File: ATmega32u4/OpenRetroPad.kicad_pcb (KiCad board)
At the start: 4 copper layers, 46 x 74 mm, 48 parts, among them J1 USB_B_Micro, J2 NRF24, J3 DB25_Female_MountingHoles, SW1 SW_Push, SW2 SW_Push, U1 AMS1117-3.3, U2 ATmega32U4, Y1 16MHz

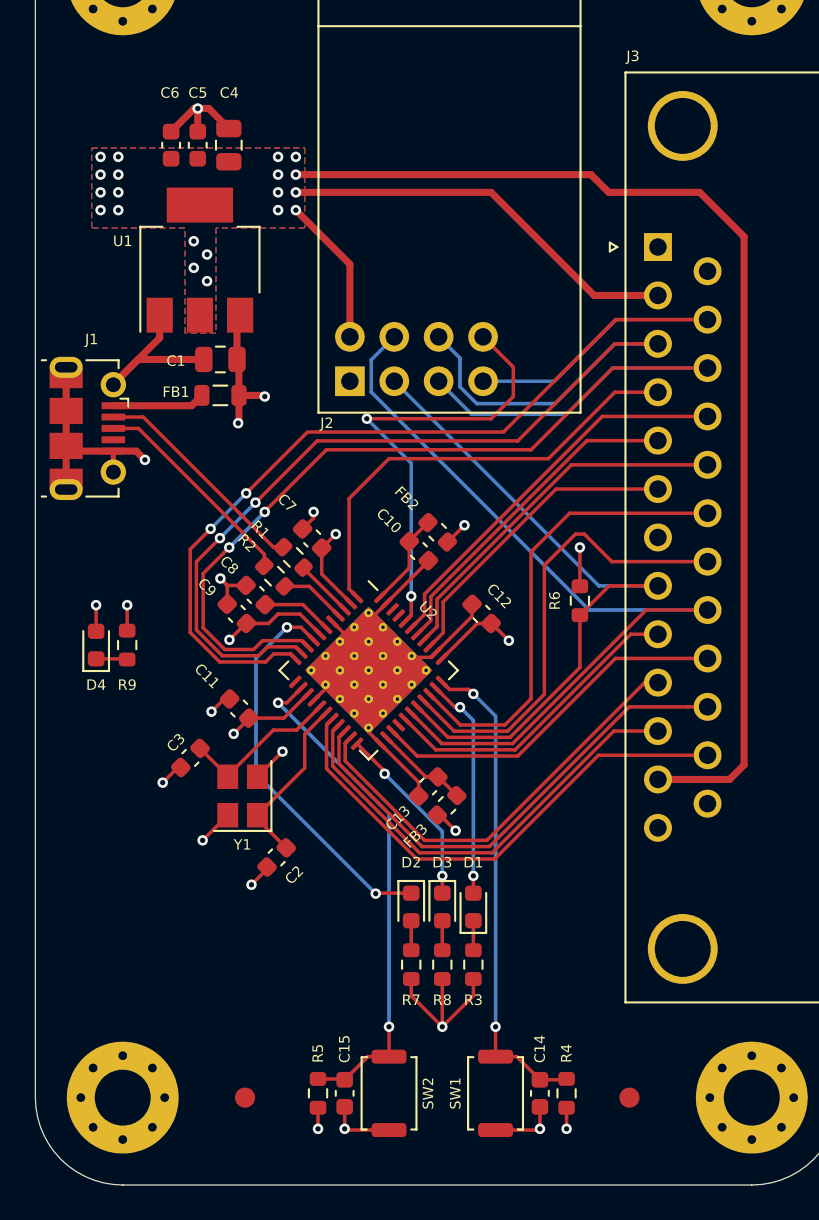
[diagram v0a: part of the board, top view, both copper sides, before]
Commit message: Update layout around MicroUSB connector, add teardrops
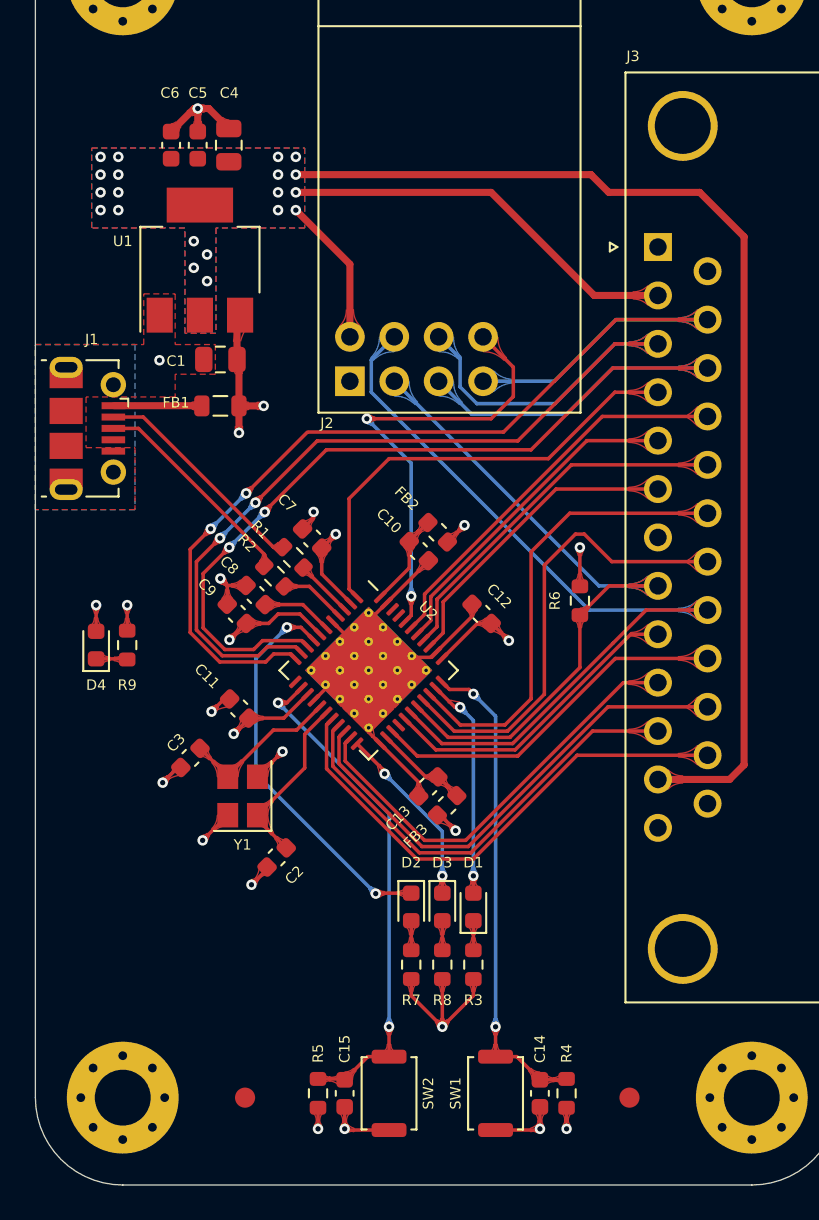
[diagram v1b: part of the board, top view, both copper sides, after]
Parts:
- moved FB1 0.60 mm to (117.3, 86.6)
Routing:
- net GND: track 91.2 -> 68.6 mm
- added copper zone on B.Cu, net GND
- added copper zone on F.Cu, net GND

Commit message: Update text on back to include domain name instead of github link
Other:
- board text added: "OpenRetroPad ATmega32u4 v1 JAN-21 OpenRetroPad.com"
- board text removed: "OpenRetroPad ATmega32u4 v1 JAN-21 github.com/OpenRetroPad"

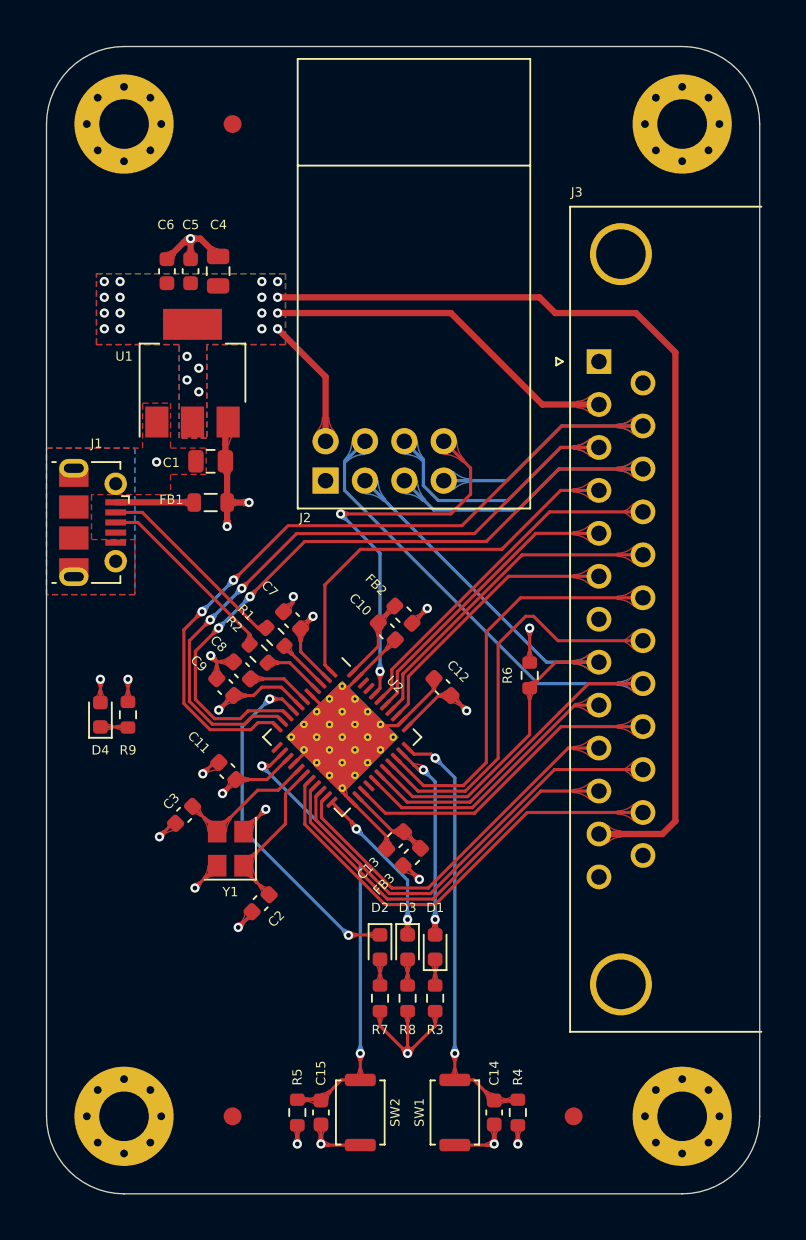
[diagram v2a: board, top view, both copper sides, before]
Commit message: Convert from 4 layer to 2 layer board
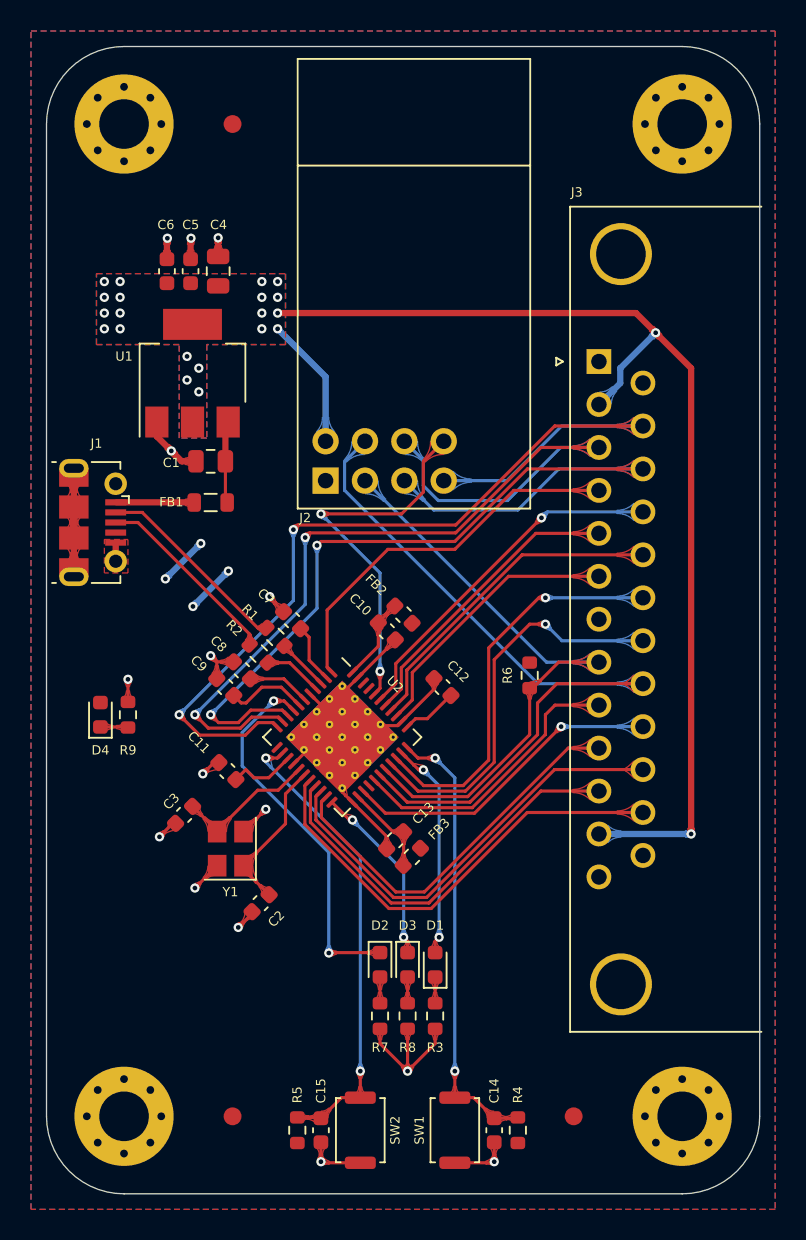
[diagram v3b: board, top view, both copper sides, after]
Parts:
- moved C14 1.14 mm to (135.6, 127.1)
- moved C15 1.14 mm to (124.5, 127.1)
- moved D1 1.14 mm to (131.8, 116.5)
- moved D2 1.14 mm to (128.3, 116.5)
- moved D3 1.14 mm to (130.0, 116.5)
- moved R3 1.14 mm to (131.8, 119.8)
- moved R4 1.14 mm to (137.2, 127.1)
- moved R5 1.14 mm to (122.9, 127.1)
- moved R7 1.14 mm to (128.3, 119.8)
- moved R8 1.14 mm to (130.0, 119.8)
- moved SW1 1.14 mm to (133.1, 127.1)
- moved SW2 1.14 mm to (127.0, 127.1)
- turned FB3 to 225 degrees
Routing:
- net +3V3: track 94.3 -> 78.8 mm, vias 20 -> 22
- net +5V: track 38.7 -> 28.9 mm, vias 12 -> 4
- net GND: track 68.6 -> 78.1 mm, vias 13 -> 15
- net PB0: track 22.7 -> 24.3 mm
- net PF1: track 25.9 -> 24.4 mm
- net PC7: track 12.8 -> 14.2 mm
- net PD5: track 10.6 -> 11.8 mm
- net PB4: track 49.0 -> 50.2 mm
- net PB1: track 61.0 -> 59.8 mm
- net PE6: track 26.0 -> 24.9 mm
- net PE2: track 28.0 -> 29.1 mm
- net RESET: track 29.2 -> 30.3 mm
- net PB3: track 61.0 -> 61.9 mm
- net PB6: track 26.6 -> 25.8 mm, vias 0 -> 1
- net PD7: track 18.0 -> 18.7 mm
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- added copper zone on F.Cu, net +5V
- removed copper zone on In2.Cu, net +5V
- removed copper zone on In1.Cu, net GND
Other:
- copper layers 4 -> 2

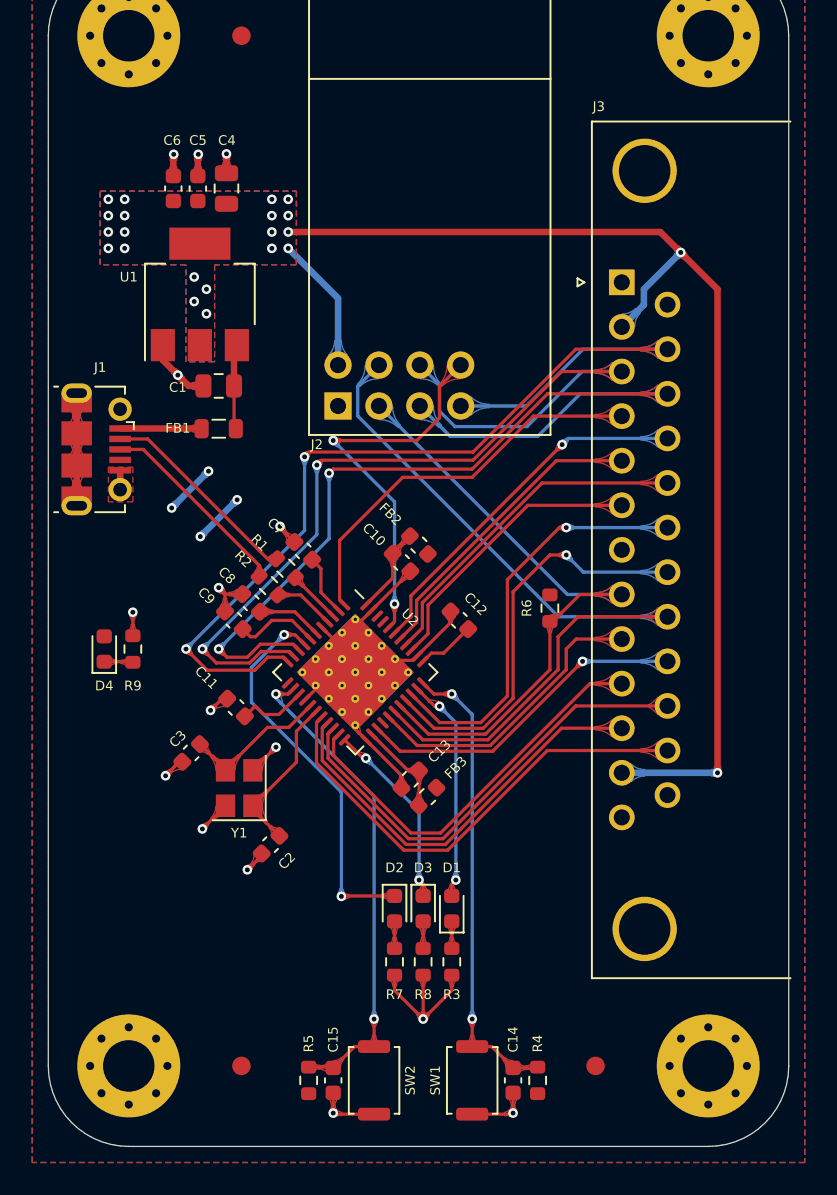
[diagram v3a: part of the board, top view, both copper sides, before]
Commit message: Update 2 layer board and use 0805 components, include outputs
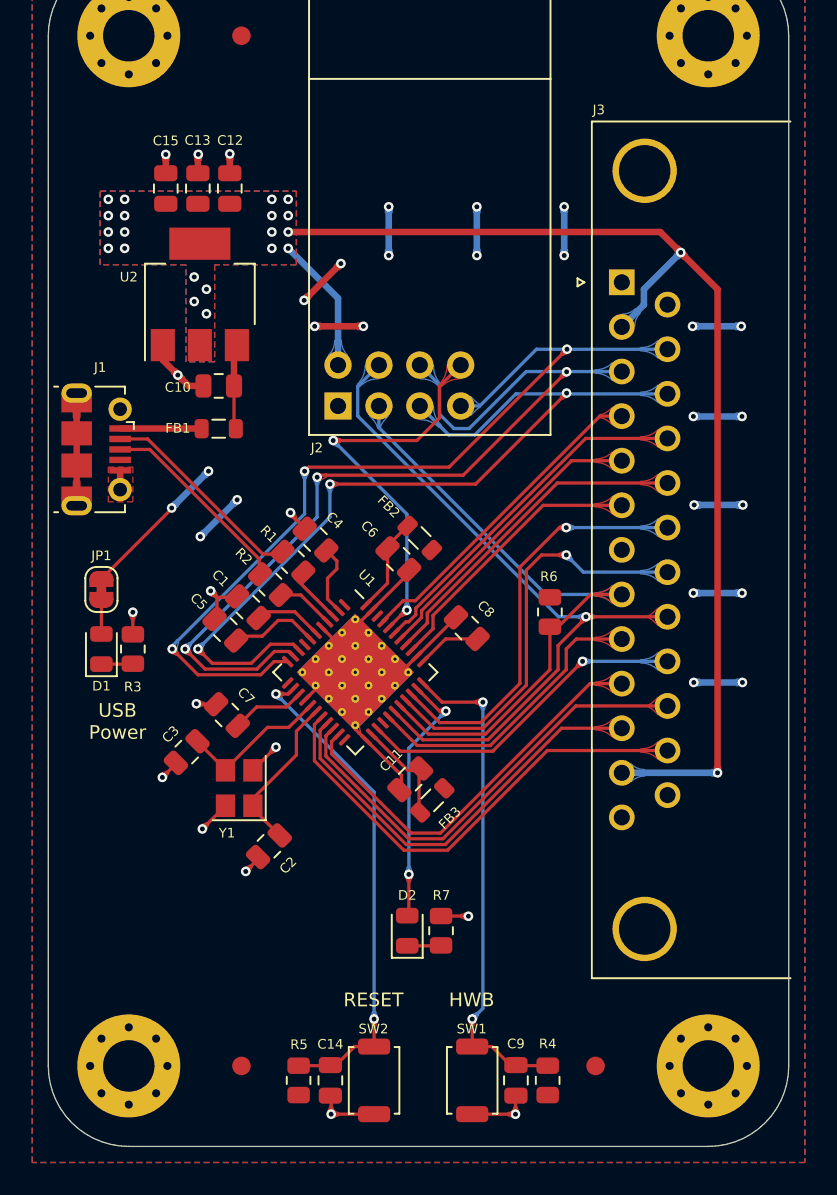
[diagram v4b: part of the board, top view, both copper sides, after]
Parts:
- removed the D1 at (131.8, 116.5)
- removed D3: RX LED, LED_SMD:LED_0603_1608Metric
- removed the R7 at (128.3, 119.8)
- removed R8: 1k, Resistor_SMD:R_0603_1608Metric
- added JP1: SJ_2_BR, Jumper:SolderJumper-2_P1.3mm_Bridged_RoundedPad1.0x1.5mm, F.Cu at (110.1, 96.6)
- C1: renamed from C8; footprint Capacitor_SMD:C_0603_1608Metric -> Capacitor_SMD:C_0805_2012Metric
- C11: renamed from C13; footprint Capacitor_SMD:C_0603_1608Metric -> Capacitor_SMD:C_0805_2012Metric
- C13: renamed from C5; footprint Capacitor_SMD:C_0603_1608Metric -> Capacitor_SMD:C_0805_2012Metric
- C14: renamed from C15; footprint Capacitor_SMD:C_0603_1608Metric -> Capacitor_SMD:C_0805_2012Metric
- C15: renamed from C6; footprint Capacitor_SMD:C_0603_1608Metric -> Capacitor_SMD:C_0805_2012Metric
- C2, C3: footprint Capacitor_SMD:C_0603_1608Metric -> Capacitor_SMD:C_0805_2012Metric
- C4: renamed from C7; footprint Capacitor_SMD:C_0603_1608Metric -> Capacitor_SMD:C_0805_2012Metric
- C5: renamed from C9; footprint Capacitor_SMD:C_0603_1608Metric -> Capacitor_SMD:C_0805_2012Metric
- C6: renamed from C10; footprint Capacitor_SMD:C_0603_1608Metric -> Capacitor_SMD:C_0805_2012Metric
- C7: renamed from C11; footprint Capacitor_SMD:C_0603_1608Metric -> Capacitor_SMD:C_0805_2012Metric
- C8: renamed from C12; footprint Capacitor_SMD:C_0603_1608Metric -> Capacitor_SMD:C_0805_2012Metric
- C9: renamed from C14; footprint Capacitor_SMD:C_0603_1608Metric -> Capacitor_SMD:C_0805_2012Metric
- D1: renamed from D4; footprint LED_SMD:LED_0603_1608Metric -> LED_SMD:LED_0805_2012Metric
- D2: value TX LED -> LED1; footprint LED_SMD:LED_0603_1608Metric -> LED_SMD:LED_0805_2012Metric
- FB2, FB3: footprint Inductor_SMD:L_0603_1608Metric -> Inductor_SMD:L_0805_2012Metric
- R1, R2, R4, R5, R6: footprint Resistor_SMD:R_0603_1608Metric -> Resistor_SMD:R_0805_2012Metric
- R3: renamed from R9; footprint Resistor_SMD:R_0603_1608Metric -> Resistor_SMD:R_0805_2012Metric
- R7: renamed from R3; footprint Resistor_SMD:R_0603_1608Metric -> Resistor_SMD:R_0805_2012Metric
- moved R7 2.04 mm to (131.2, 117.8), turned to 270 degrees
- moved D2 1.58 mm to (129.1, 117.8), turned to 90 degrees
- moved C4 1.04 mm to (123.4, 93.5)
- moved C5 0.79 mm to (117.8, 99.1)
- moved C7 0.73 mm to (117.9, 104.4)
- moved C8 0.67 mm to (132.8, 99.0)
- moved R5 0.63 mm to (122.3, 127.1)
- moved R4 0.62 mm to (137.8, 127.1)
- moved R1 0.58 mm to (122.0, 94.9)
- moved C15 0.47 mm to (114.1, 71.7)
- moved FB2 0.45 mm to (129.8, 93.4)
- moved FB3 0.37 mm to (130.6, 109.7)
- moved C1 0.34 mm to (119.2, 97.7)
- moved C6 0.28 mm to (128.5, 94.8)
- moved C3 0.28 mm to (115.4, 106.7)
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- renumbered C1 to C10, C4 to C12, LOGO2 to LOGO1, LOGO1 to LOGO2, U2 to U1, U1 to U2
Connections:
- D1 pad 2: +5V -> Net-(D1-Pad2)
- D2 pad 1: PB0 -> Net-(D2-Pad1)
- D2 pad 2: Net-(D2-Pad2) -> PC7
- J3 pad 4: PE6 -> PF0
- R7 pad 2: Net-(D1-Pad1) (its old number) -> Net-(D2-Pad1)
- U1 pad 1: PE6 -> Net-(U1-Pad1)
- U1 pad 22: PD5 -> Net-(U1-Pad22)
- U1 pad 41: Net-(U2-Pad41) -> PF0
- U1 pad 8: PB0 -> Net-(U1-Pad8)
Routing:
- net +5V: track 28.9 -> 60.9 mm, vias 4 -> 20
- net PE6: track 24.9 -> 0.00 mm
- net PB0: track 24.3 -> 0.00 mm, vias 2 -> 0
- net PF0: track 0.00 -> 20.2 mm
- net PD5: track 11.8 -> 0.00 mm, vias 2 -> 0
- net PB3: track 61.9 -> 56.4 mm, vias 2 -> 3
- net PB4: track 50.2 -> 44.8 mm, vias 0 -> 1
- net PB1: track 59.8 -> 55.2 mm, vias 2 -> 3
- net GND: track 78.1 -> 73.9 mm, vias 15 -> 19
- net Net-(D1-Pad2): track 0.00 -> 2.11 mm
- net Net-(D2-Pad1): track 0.00 -> 2.11 mm
- net PE2: track 29.1 -> 31.1 mm
- net PC7: track 14.2 -> 16.1 mm
- net PB2: track 58.7 -> 56.9 mm, vias 2 -> 3
- net Net-(D3-Pad2): track 1.69 -> 0.00 mm
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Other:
- board text added: "- - - D14 D16 D15 D23 D21 D20 D19 D18 D5 - D10 D9 D8 D6 D4 D1 D0 D2 D3 - - -"
- board text added: "- - - MISO MOSI SCK A5 A3 A2 A1 A0 - - A10 A9 A8 A7 A6 TX RX SDA SCL - - -"
- board text added: "3V3 GND"
- board text added: "Alt"
- board text added: "GND 5V 3V3 PB3 PB2 PB1 PF0 PF4 PF5 PF6 PF7 PC6 - PB6 PB5 PB4 PD7 PD4 PD3 PD2 PD1 PD0 3V3 5V GND"
- board text added: "HWB"
- board text added: "Leonardo"
- board text added: "OpenRetroPad ATmega32u4 v1 JAN-2021 OpenRetroPad.com"
- board text added: "PB2 PB1"
- board text added: "PB4 PB5"
- board text added: "PF1 PB3"
- board text added: "RESET"
- board text added: "USB Power"
- board text removed: "- - - 14 16 15 7 21 20 19 18 5 - 10 9 8 6 4 1 0 2 3 - - -"
- board text removed: "Arduino"
- board text removed: "GND 5V 3V3 PB3 PB2 PB1 PE6 PF4 PF5 PF5 PF7 PC6 - PB6 PB5 PB4 PD7 PD4 PD3 PD2 PD1 PD0 3V3 5V GND"
- board text removed: "JLCJLCJLCJLC"
- board text removed: "OpenRetroPad ATmega32u4 v1 JAN-21 OpenRetroPad.com"
